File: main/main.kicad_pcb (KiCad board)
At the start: 4 copper layers, 65 x 70.8 mm, 18 parts, among them J1 Conn_01x18_Female, U1 ATmega1284P-PU

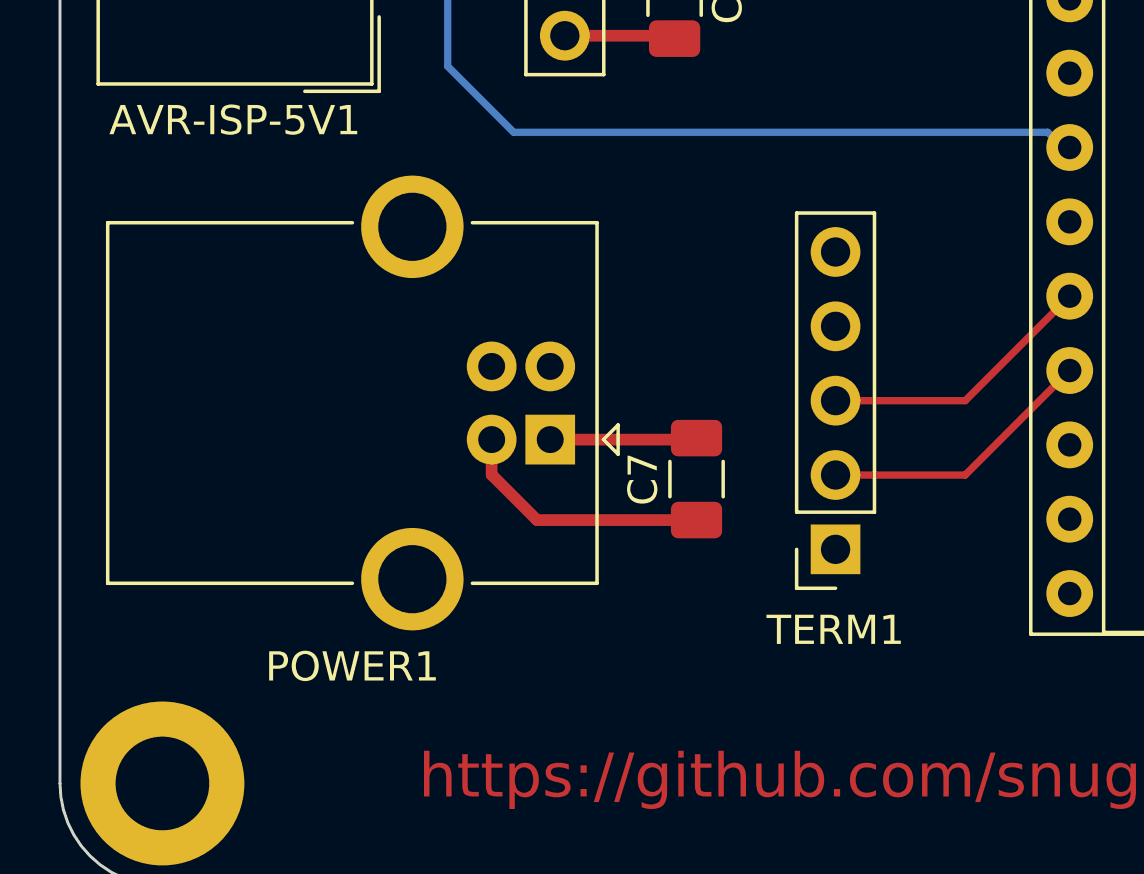
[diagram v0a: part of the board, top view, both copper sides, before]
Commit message: removed unnecessary usb-b port
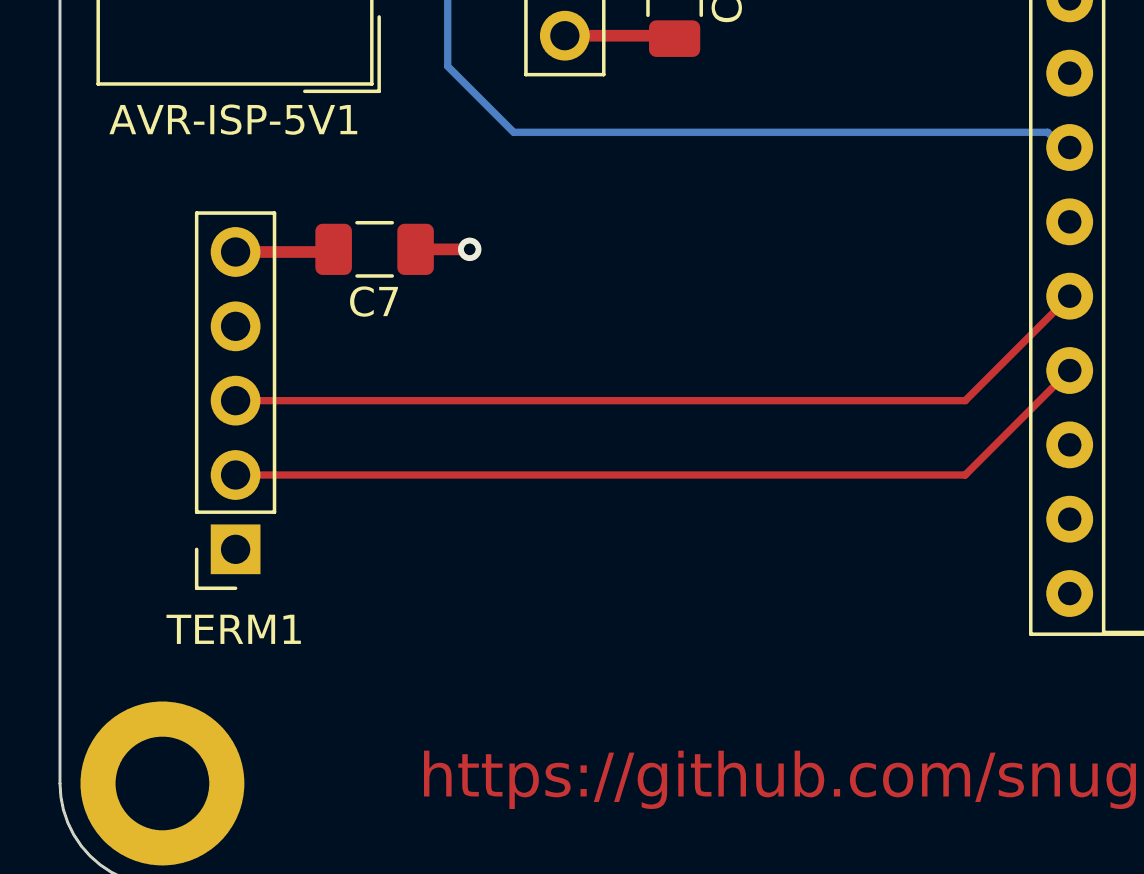
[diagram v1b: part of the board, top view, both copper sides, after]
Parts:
- removed POWER1: USB_B, Connector_USB:USB_B_OST_USB-B1HSxx_Horizontal
- moved TERM1 20.5 mm to (76.5, 116.0)
- moved C7 13.5 mm to (81.2, 105.8), turned to 180 degrees
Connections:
- TERM1 pad 4: Net-(TERM1-Pad4) -> (no net)
- U1 pad 1: Net-(U1-Pad1) -> (no net)
- U1 pad 12: Net-(U1-Pad12) -> (no net)
- U1 pad 13: Net-(U1-Pad13) -> (no net)
- U1 pad 15: Net-(U1-Pad15) -> (no net)
- U1 pad 18: Net-(U1-Pad18) -> (no net)
- U1 pad 19: Net-(U1-Pad19) -> (no net)
- U1 pad 2: Net-(U1-Pad2) -> (no net)
- U1 pad 20: Net-(U1-Pad20) -> (no net)
- U1 pad 21: Net-(U1-Pad21) -> (no net)
- U1 pad 3: Net-(U1-Pad3) -> (no net)
- U1 pad 4: Net-(U1-Pad4) -> (no net)
- U1 pad 5: Net-(U1-Pad5) -> (no net)
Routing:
- net UTX: track 9.48 -> 30.0 mm
- net URX: track 9.65 -> 30.1 mm
- net GND: track 24.7 -> 17.7 mm, vias 0 -> 1
- net +5V: track 28.8 -> 27.2 mm
